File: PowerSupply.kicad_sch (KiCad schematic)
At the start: 51 parts, among them CN1 SM04B-SRSS-TB (LF)(SN), Q1 CSD17318Q2, Q2 CSD17318Q2, U1 TPS55288RPMR

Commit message: Added to pcb
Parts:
- removed L4: IHLP2020CZER4R7M11, 2020, symbol Device:L
- removed Q1, Q2: CSD17318Q2, Package_TO_SOT_SMD:TDSON-8-1, symbol Transistor_FET:CSD17310Q5A
- removed R22: PTFR0603B113KP9, easyeda2kicad:R0603, symbol easyeda2kicad:0603WAF1003T5E
- added H1, H2, H3, H4: MountingHole_Pad, MountingHole:MountingHole_2.2mm_M2_Pad, symbol Mechanical:MountingHole_Pad
- added L4: CYA0630-4.7UH, easyeda2kicad:IND-SMD_L7.2-W6.6_GPSR07X0, symbol easyeda_symbole:CYA0630-4.7UH
- added Q1, Q2: CSD17318Q2, easyeda2kicad:WSON-6_L2.0-W2.0-P0.65-TL_CSD19538Q2, symbol easyeda_symbole:CSD17318Q2
- added R22: RT0603BRD07113KL, easyeda2kicad:R0603, symbol easyeda_symbole:RT0603BRD07113KL
- TP47: footprint (none) -> TestPoint:TestPoint_Pad_1.5x1.5mm
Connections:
- net DR1H_R: now also Q1.3 (G)
- net GND: now also H1.1, H2.1, H3.1, H4.1
- net GND_PURPLE: now also Q2.4 (S), Q2.7 (S), R22.1
- net TPS_SW1: now also L4.1, Q1.4 (S), Q1.7 (S), Q2.1 (D), Q2.2 (D), Q2.5 (D), Q2.6 (D), Q2.8 (D)
- net TPS_SW2: now also L4.2
- net VIN: now reaches C25.2, C314.2, R47.2, TP38.1, TP47.1, U1.3 (VIN)
- net VIN: now also Q1.1 (D), Q1.2 (D), Q1.5 (D), Q1.6 (D), Q1.8 (D)
- net at R2.2: now also Q2.3 (G)
- net at C28.1: now also R22.2
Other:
- moved on the sheet: R1, TP47, TP6, TP7

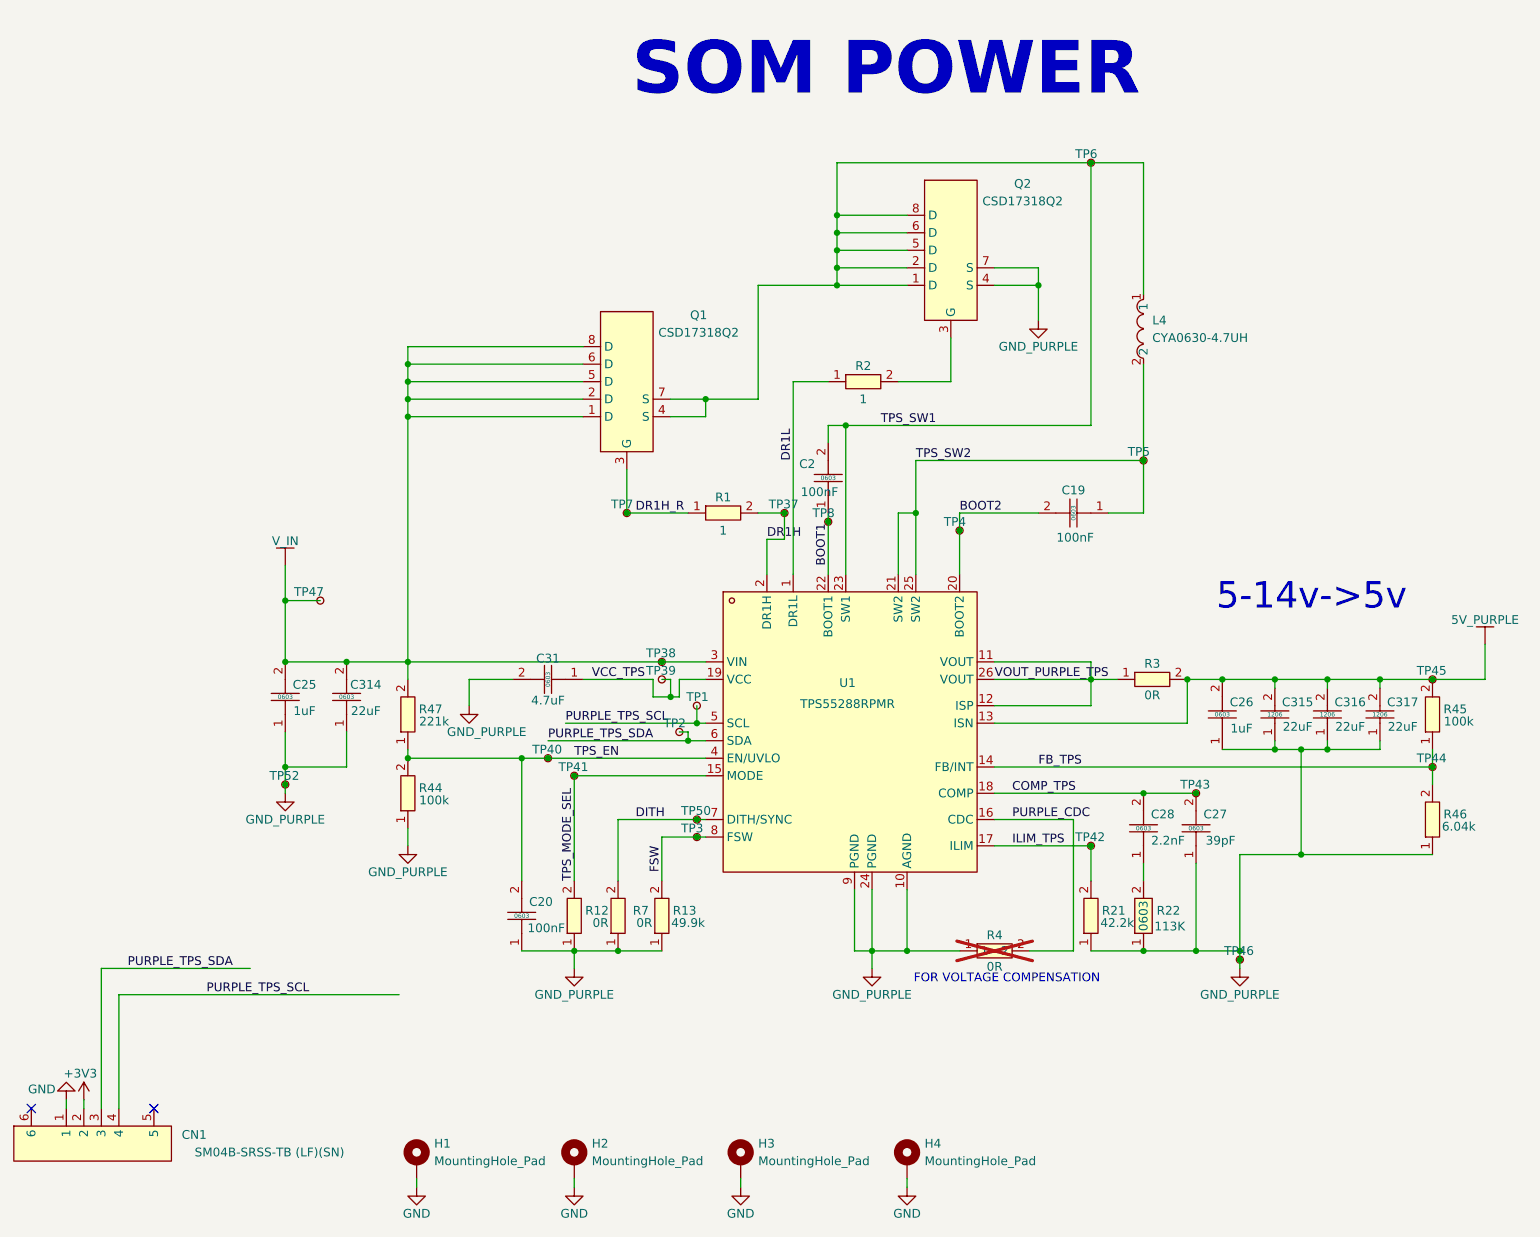
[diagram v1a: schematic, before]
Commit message: Removed TP
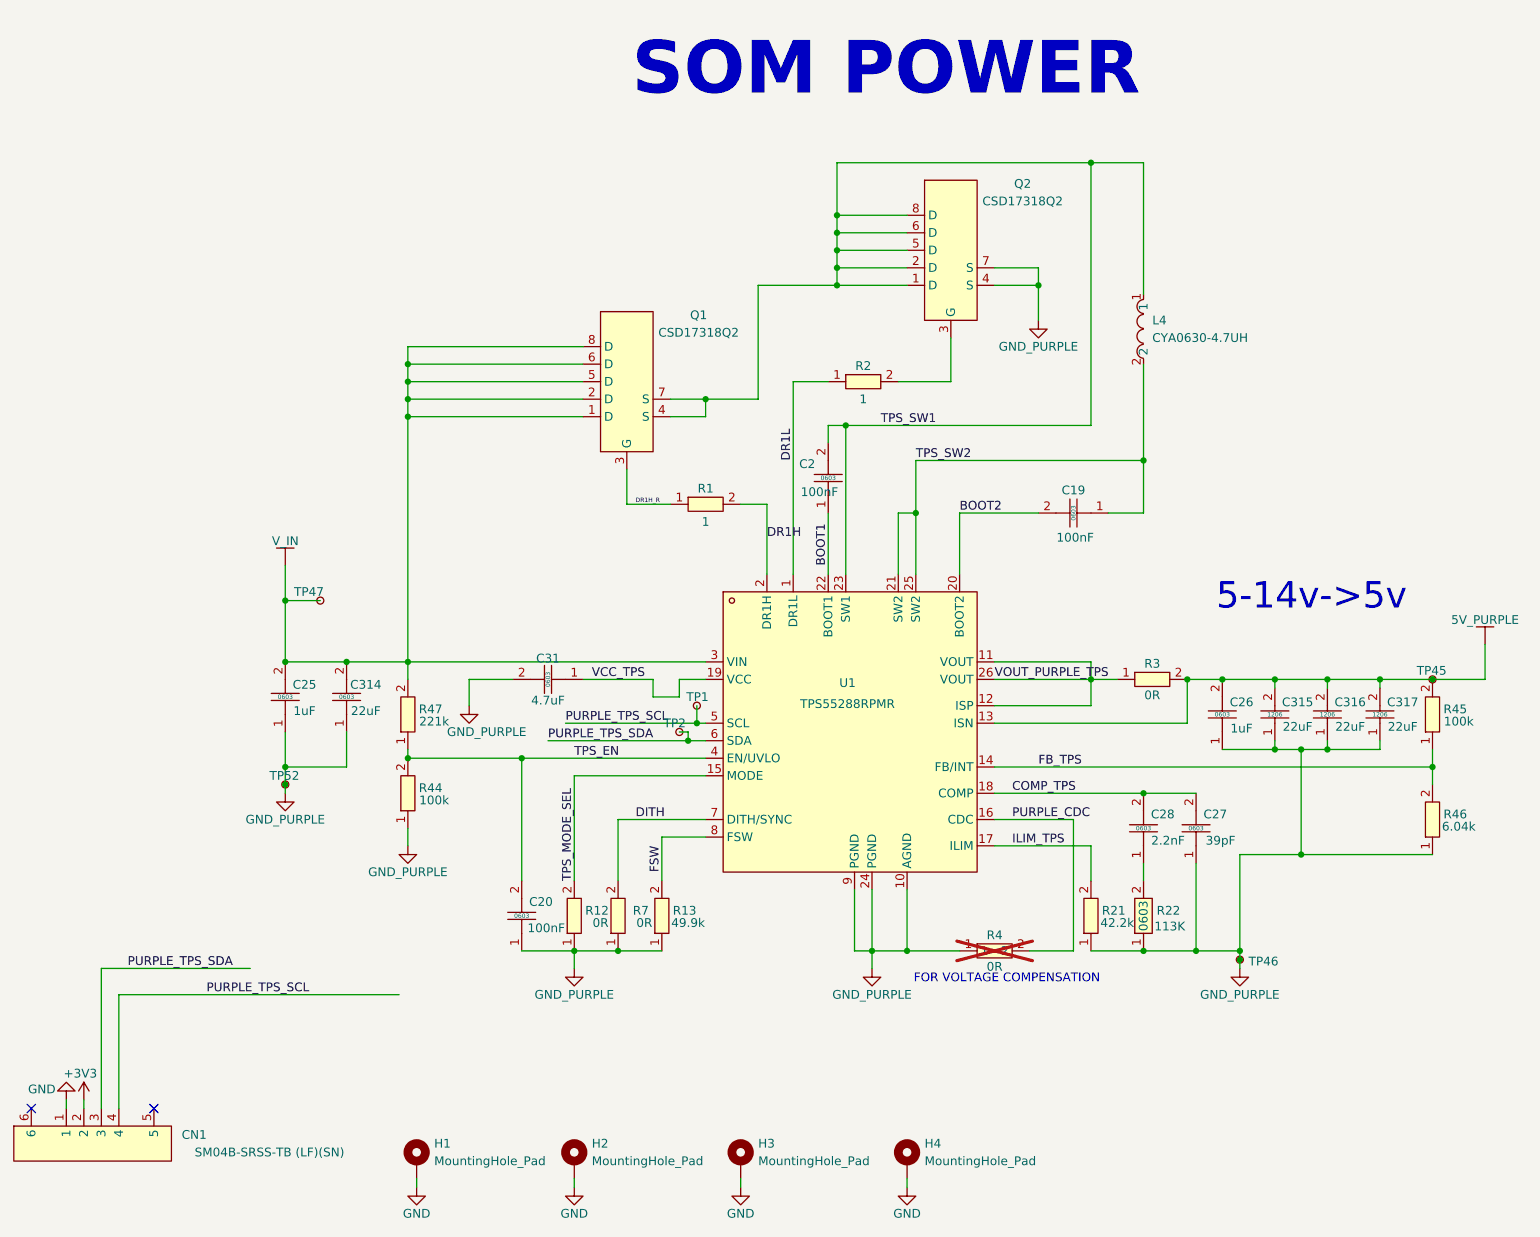
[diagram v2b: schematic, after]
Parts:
- removed TP3, TP37, TP38, TP39, TP4, TP40, TP41, TP42, TP43, TP44, TP5, TP50, TP6, TP7, TP8: TestPoint_Small, symbol Connector:TestPoint_Small
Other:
- moved on the sheet: R1
